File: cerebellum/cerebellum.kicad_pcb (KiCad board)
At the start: 2 copper layers, 0 parts

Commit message: [Complete cerebellum schematic
* add gd32f405vghx to library

Signed-off-by: Homalozoa X <nx.tardis@gmail.com>
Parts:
- added C1: 20pF, 10%, 10V, Capacitor_SMD:C_0402_1005Metric, B.Cu at (138.7, 115.8)
- added C10: 100nF, 10%, 10V, Capacitor_SMD:C_0402_1005Metric, B.Cu at (136.1, 106.1)
- added C11: 10uF, 10%, 10V, Capacitor_SMD:C_0402_1005Metric, B.Cu at (137.5, 122.5)
- added C12: 100nF, 10%, 10V, Capacitor_SMD:C_0402_1005Metric, B.Cu at (138.6, 122.5)
- added C13: 4.7uF 50V, Capacitor_SMD:C_0805_2012Metric, B.Cu at (121.2, 78.4)
- added C14: 10pF, 10%, 50V, Capacitor_SMD:C_0402_1005Metric, B.Cu at (125.8, 113.3)
- added C15: 10pF, 10%, 50V, Capacitor_SMD:C_0402_1005Metric, B.Cu at (125.8, 108.2)
- added C16: 10nF, 10%, 50V, Capacitor_SMD:C_0402_1005Metric, B.Cu at (119.1, 107.8)
- added C17: 10nf 50V, Capacitor_SMD:C_0402_1005Metric, B.Cu at (124.3, 98.7)
- added C18: 470nF, 10%, 50V, Capacitor_SMD:C_0603_1608Metric, B.Cu at (123.3, 107.7)
- added C19: 100uf 50V, Capacitor_SMD:C_0805_2012Metric, B.Cu at (120.7, 100.2)
- added C2: 100nF, 10%, 10V, Capacitor_SMD:C_0402_1005Metric, B.Cu at (138.0, 113.4)
- added C20: 100nf 10V, Capacitor_SMD:C_0402_1005Metric, B.Cu at (136.1, 109.2)
- added C21: 1.5nf 50V, Capacitor_SMD:C_0402_1005Metric, B.Cu at (117.1, 96.9)
- added C22: 100pF, 10%, 10V, Capacitor_SMD:C_0402_1005Metric, B.Cu at (116.4, 111.9)
- added C23: 100pF, 10%, 10V, Capacitor_SMD:C_0402_1005Metric, B.Cu at (116.4, 109.2)
- added C24: 100nf 50V, Capacitor_SMD:C_0402_1005Metric, B.Cu at (118.1, 98.8)
- added C25: 100nF, 10%, 50V, Capacitor_SMD:C_0402_1005Metric, B.Cu at (120.2, 105.8)
- added C26: 10uF, 10%, 50V, Capacitor_SMD:C_0603_1608Metric, B.Cu at (119.8, 104.5)
- added C27: 10uF, 10%, 50V, Capacitor_SMD:C_0603_1608Metric, B.Cu at (123.3, 106.2)
- added C28: 150pf 50V, Capacitor_SMD:C_0402_1005Metric, B.Cu at (115.0, 98.9)
- added C29: 4.7uF, 10%, 10V, Capacitor_SMD:C_0402_1005Metric, B.Cu at (177.8, 102.8)
- added C3: 20pF, 10%, 10V, Capacitor_SMD:C_0402_1005Metric, B.Cu at (138.8, 120.9)
- added C30: 100nF, 10%, 10V, Capacitor_SMD:C_0402_1005Metric, B.Cu at (176.7, 102.8)
- added C31: 4.7uF, 10%, 10V, Capacitor_SMD:C_0402_1005Metric, B.Cu at (120.6, 119.5)
- added C32: 100nF, 10%, 10V, Capacitor_SMD:C_0402_1005Metric, B.Cu at (120.6, 118.2)
- added C4: 100nF, 10%, 10V, Capacitor_SMD:C_0402_1005Metric, B.Cu at (136.0, 112.3)
- added C5: 100nF, 10%, 10V, Capacitor_SMD:C_0402_1005Metric, B.Cu at (136.0, 111.3)
- added C6: 4.7uF, 10%, 10V, Capacitor_SMD:C_0402_1005Metric, B.Cu at (136.0, 110.3)
- added C7: 1uF, 10%, 10V, Capacitor_SMD:C_0402_1005Metric, B.Cu at (136.1, 107.2)
- added C8: 100nF, 10%, 10V, Capacitor_SMD:C_0402_1005Metric, B.Cu at (136.1, 108.2)
- added C9: 10uF, 10%, 10V, Capacitor_SMD:C_0402_1005Metric, B.Cu at (136.1, 105.1)
- added D1: 30V, Diode_SMD:D_SMA, B.Cu at (121.3, 81.2)
- added D2: B340, Diode_SMD:D_SMC, B.Cu at (129.3, 96.7)
- added D3: 12V, Diode_SMD:D_SOD-323, B.Cu at (114.9, 112.5)
- added D4: 12V, Diode_SMD:D_SOD-323, B.Cu at (114.9, 108.5)
- added J1: PWR_OUT, Rolling_Custom:XT30PW(2+2), F.Cu at (119.3, 85.9)
- added J2: PWR_IN, Rolling_Custom:XT30PW(2+2), F.Cu at (134.0, 85.9)
- added J3: Conn_01x04, Connector_PinHeader_1.27mm:PinHeader_1x04_P1.27mm_Vertical, F.Cu at (157.2, 76.0)
- added J4: gh1.25, 3p, Connector_JST:JST_GH_SM03B-GHS-TB_1x03-1MP_P1.25mm_Horizontal, F.Cu at (148.5, 77.6)
- added L1: 20R, Resistor_SMD:R_0402_1005Metric, B.Cu at (137.0, 124.0)
- added L2: 15uh, Inductor_SMD:L_0603_1608Metric, B.Cu at (124.1, 100.0)
- added Q1: AP2300, Package_TO_SOT_SMD:SOT-23, B.Cu at (172.8, 104.7)
- added R1: 10k, 5%, Resistor_SMD:R_0402_1005Metric, B.Cu at (136.0, 113.4)
- added R10: 10k, Resistor_SMD:R_0402_1005Metric, B.Cu at (175.5, 103.9)
- added R11: 549R, Resistor_SMD:R_0201_0603Metric, B.Cu at (116.0, 98.7)
- added R12: 33R/1%, Resistor_SMD:R_0805_2012Metric, B.Cu at (172.9, 93.3)
- added R13: 33R/1%, Resistor_SMD:R_0805_2012Metric, B.Cu at (177.3, 89.4)
- added R14: 33R/1%, Resistor_SMD:R_0805_2012Metric, B.Cu at (177.4, 97.2)
- added R15: 33R/1%, Resistor_SMD:R_0805_2012Metric, B.Cu at (181.8, 93.3)
- added R2: 10k, 5%, Resistor_SMD:R_0402_1005Metric, B.Cu at (133.2, 113.5)
- added R3: 0, Resistor_SMD:R_0402_1005Metric, B.Cu at (139.6, 122.5)
- added R4: 33k, Resistor_SMD:R_0402_1005Metric, B.Cu at (117.4, 106.8)
- added R5: 3k, Resistor_SMD:R_0402_1005Metric, B.Cu at (120.1, 106.8)
- added R6: 10k, Resistor_SMD:R_0402_1005Metric, B.Cu at (118.1, 96.9)
- added R7: 5.9k, Resistor_SMD:R_0402_1005Metric, B.Cu at (116.0, 96.9)
- added R9: 100R, Resistor_SMD:R_0402_1005Metric, B.Cu at (173.0, 102.3)
- added U1: GD32F405VGHx, Package_BGA:UFBGA-100_7x7mm_Layout12x12_P0.5mm, B.Cu at (132.4, 118.6)
- added U2: TPS5430DDAR, Rolling_Custom:TPS5430DDAR, B.Cu at (121.5, 93.7)
- added U3: BMI088, Rolling_Custom:PQFN50P450X300X100-16N, B.Cu at (177.4, 93.3)
- added U4: TCAN4550RGYRQ1, Rolling_Custom:VQFN20, B.Cu at (120.7, 110.7)
- added U5: ICP-20100, Rolling_Custom:PQFN50P200X200X85-10N, B.Cu at (120.3, 121.5)
- added Y1: 8M, Oscillator:Oscillator_SMD_EuroQuartz_XO32-4Pin_3.2x2.5mm, B.Cu at (138.7, 118.3)
- added Y2: 40M, Oscillator:Oscillator_SMD_EuroQuartz_XO32-4Pin_3.2x2.5mm, B.Cu at (125.8, 110.7)
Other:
- board outline added: 91.5 x 52 mm

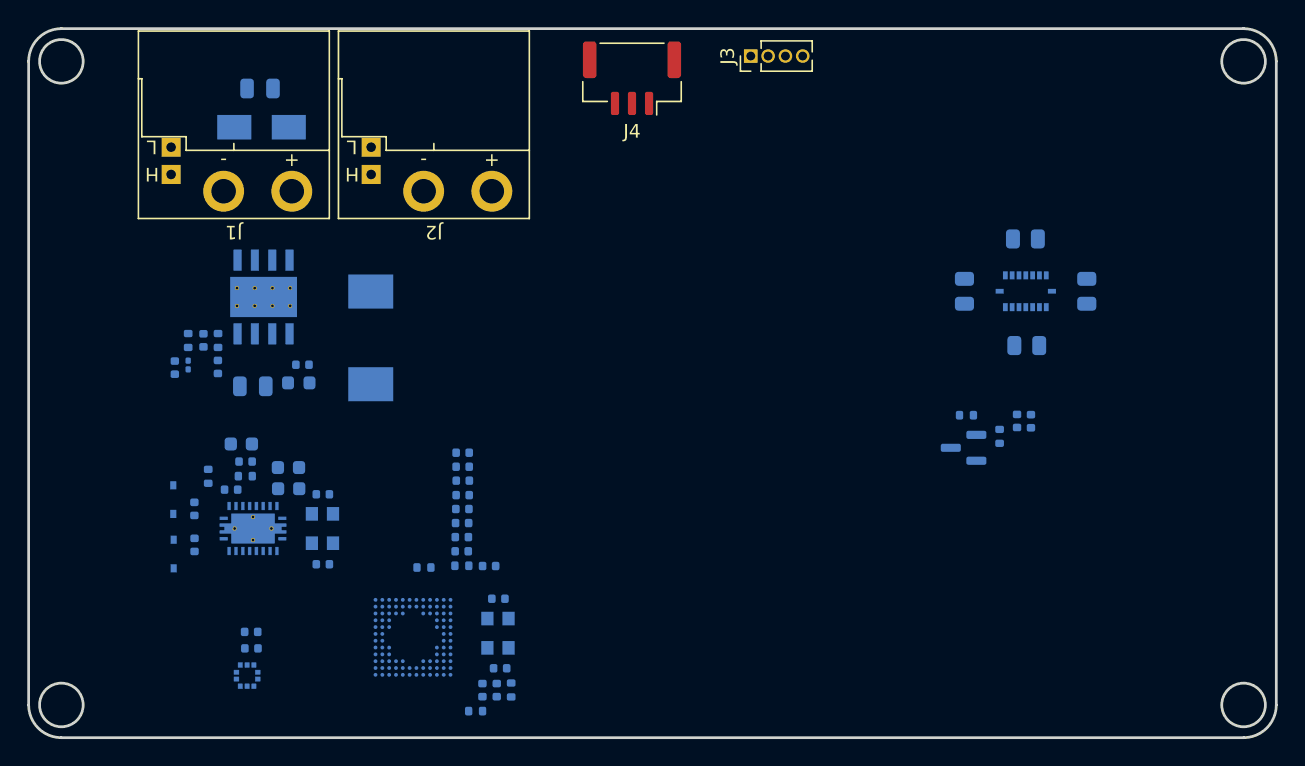
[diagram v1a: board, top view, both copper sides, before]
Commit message: [New] Add cm4 to cerebellum
Signed-off-by: Homalozoa X <nx.tardis@gmail.com>
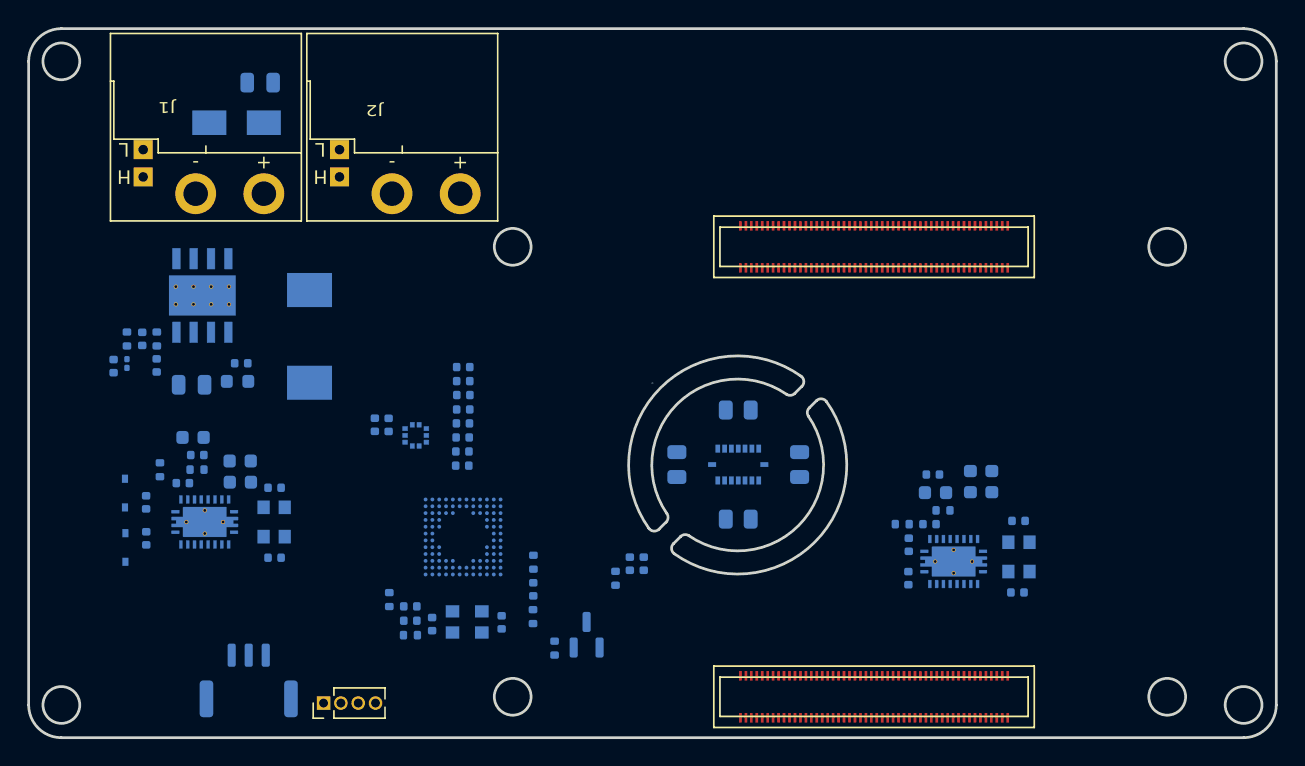
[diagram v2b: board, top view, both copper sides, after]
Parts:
- added C33: 10pF, 10%, 50V, Capacitor_SMD:C_0402_1005Metric, B.Cu at (176.8, 115.3)
- added C34: 10pF, 10%, 50V, Capacitor_SMD:C_0402_1005Metric, B.Cu at (176.8, 110.1)
- added C35: 10nF, 10%, 50V, Capacitor_SMD:C_0402_1005Metric, B.Cu at (170.3, 110.3)
- added C36: 470nF, 10%, 50V, Capacitor_SMD:C_0603_1608Metric, B.Cu at (174.9, 107.2)
- added C37: 100pF, 10%, 10V, Capacitor_SMD:C_0402_1005Metric, B.Cu at (168.8, 114.3)
- added C38: 100pF, 10%, 10V, Capacitor_SMD:C_0402_1005Metric, B.Cu at (168.8, 111.8)
- added C39: 100nF, 10%, 50V, Capacitor_SMD:C_0402_1005Metric, B.Cu at (170.6, 106.7)
- added C40: 10uF, 10%, 50V, Capacitor_SMD:C_0603_1608Metric, B.Cu at (170.8, 108.0)
- added C41: 10uF, 10%, 50V, Capacitor_SMD:C_0603_1608Metric, B.Cu at (173.3, 107.2)
- added J5: DF40C-100DS-0.4V(51), Rolling_Custom:HRS_DF40C-100DS-0.4V(51), F.Cu at (166.2, 123.0)
- added J6: DF40C-100DS-0.4V(51), Rolling_Custom:HRS_DF40C-100DS-0.4V(51), F.Cu at (166.2, 90.0)
- added R16: 3k, Resistor_SMD:R_0402_1005Metric, B.Cu at (171.3, 109.3)
- added R8: 33k, Resistor_SMD:R_0402_1005Metric, B.Cu at (168.3, 110.3)
- added U7: TCAN4550RGYRQ1, Rolling_Custom:VQFN20, B.Cu at (172.1, 113.1)
- added Y3: 40M, Oscillator:Oscillator_SMD_EuroQuartz_XO32-4Pin_3.2x2.5mm, B.Cu at (176.9, 112.7)
- J4: moved to B.Cu
- moved J3 56.9 mm to (125.9, 123.5)
- moved J4 52.4 mm to (120.4, 121.8)
- moved R9 34.7 mm to (142.8, 119.4), turned to 90 degrees
- moved Q1 30.9 mm to (145.2, 118.5), turned to 90 degrees
- moved C30 30.3 mm to (148.3, 113.2)
- moved C29 30.3 mm to (149.4, 113.2)
- moved R10 30.0 mm to (147.3, 114.3)
- moved R13 29.4 mm to (156.3, 110.0), turned to 180 degrees
- moved U3 24.6 mm to (156.3, 106.0)
- moved R12 24.6 mm to (151.8, 106.0)
- moved R15 24.6 mm to (160.8, 106.0)
- moved R14 21.7 mm to (156.3, 102.0), turned to 0 degrees
- moved U5 21.5 mm to (132.6, 103.8), turned to -90 degrees
- moved C31 19.2 mm to (130.7, 103.1), turned to -90 degrees
- moved C32 17.7 mm to (129.6, 103.0), turned to -90 degrees
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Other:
- outline, holes or cut-outs redrawn
- copper layers 2 -> 4

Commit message: [New] NC serveral pins of CM4 & Add uPD720201
Signed-off-by: Homalozoa X <nx.tardis@gmail.com>
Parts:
- moved C38 33.0 mm to (159.3, 80.2), turned to -90 degrees
- moved C33 31.3 mm to (168.5, 85.2)
- moved C35 31.3 mm to (162.0, 80.2)
- moved C36 31.3 mm to (166.6, 77.1)
- moved C39 31.3 mm to (162.3, 76.5)
- moved C40 31.3 mm to (162.5, 77.9)
- moved C41 31.3 mm to (165.0, 77.1)
- moved C34 31.3 mm to (168.6, 80.0)
- moved R16 31.3 mm to (163.0, 79.2)
- moved U7 31.3 mm to (163.8, 82.9)
- moved Y3 31.3 mm to (168.6, 82.6)
- moved C37 30.5 mm to (159.4, 85.3), turned to 90 degrees
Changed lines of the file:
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@@
   )
   (footprint "Capacitor_SMD:C_0402_1005Metric" (layer "B.Cu")
-    (at 170.3175 110.34)
+    (at 162.03 80.19)
     (descr "Capacitor SMD 0402 (1005 Metric), square (rectangular) end terminal, IPC_7351 nominal, (Body size source: IPC-SM-782 page 76, https://www.pcb-3d.com/wordpress/wp-content/uploads/ipc-sm-782a_amendment_1_and_2.pdf), generated with kicad-footprint-generator")
     (tags "capacitor")
@@
   )
   (footprint "Resistor_SMD:R_0402_1005Metric" (layer "B.Cu")
-    (at 171.3075 109.33 180)
+    (at 163.02 79.18 180)
     (descr "Resistor SMD 0402 (1005 Metric), square (rectangular) end terminal, IPC_7351 nominal, (Body size source: IPC-SM-782 page 72, https://www.pcb-3d.com/wordpress/wp-content/uploads/ipc-sm-782a_amendment_1_and_2.pdf), generated with kicad-footprint-generator")
     (tags "resistor")
@@
   )
   (footprint "Oscillator:Oscillator_SMD_EuroQuartz_XO32-4Pin_3.2x2.5mm" (layer "B.Cu")
-    (at 176.8775 112.74)
+    (at 168.59 82.59)
     (descr "Miniature Crystal Clock Oscillator EuroQuartz XO32 series, http://cdn-reichelt.de/documents/datenblatt/B400/XO32.pdf, 3.2x2.5mm^2 package")
     (tags "SMD SMT crystal oscillator")
@@
   )
   (footprint "Rolling_Custom:VQFN20" (layer "B.Cu")
-    (at 172.09 113.08 90)
+    (at 163.8025 82.93 90)
     (property "MANUFACTURER" "Texas Instruments")
     (property "MAXIMUM_PACKAGE_HEIGHT" "1 mm")
@@
       (effects (font (size 1 1) (thickness 0.15)) (justify mirror))
     )
-    (fp_text user "${REFERENCE}" (at 0 0) (layer "B.SilkS")
+    (fp_text user "${REFERENCE}" (at 0.0075 -0.06) (layer "B.SilkS")
       (effects (font (size 0.8 0.26) (thickness 0.04)) (justify mirror))
     )
@@
   )
   (footprint "Capacitor_SMD:C_0402_1005Metric" (layer "B.Cu")
-    (at 176.8475 110.1)
+    (at 168.56 79.95)
     (descr "Capacitor SMD 0402 (1005 Metric), square (rectangular) end terminal, IPC_7351 nominal, (Body size source: IPC-SM-782 page 76, https://www.pcb-3d.com/wordpress/wp-content/uploads/ipc-sm-782a_amendment_1_and_2.pdf), generated with kicad-footprint-generator")
     (tags "capacitor")
@@
   )
   (footprint "Capacitor_SMD:C_0603_1608Metric" (layer "B.Cu")
-    (at 174.8875 107.22 90)
+    (at 166.6 77.07 90)
     (descr "Capacitor SMD 0603 (1608 Metric), square (rectangular) end terminal, IPC_7351 nominal, (Body size source: IPC-SM-782 page 76, https://www.pcb-3d.com/wordpress/wp-content/uploads/ipc-sm-782a_amendment_1_and_2.pdf), generated with kicad-footprint-generator")
     (tags "capacitor")
@@
   )
   (footprint "Capacitor_SMD:C_0402_1005Metric" (layer "B.Cu")
-    (at 176.7675 115.35 180)
+    (at 168.48 85.2 180)
     (descr "Capacitor SMD 0402 (1005 Metric), square (rectangular) end terminal, IPC_7351 nominal, (Body size source: IPC-SM-782 page 76, https://www.pcb-3d.com/wordpress/wp-content/uploads/ipc-sm-782a_amendment_1_and_2.pdf), generated with kicad-footprint-generator")
     (tags "capacitor")
@@
   )
   (footprint "Capacitor_SMD:C_0402_1005Metric" (layer "B.Cu")
-    (at 170.5675 106.7 180)
+    (at 162.28 76.55 180)
     (descr "Capacitor SMD 0402 (1005 Metric), square (rectangular) end terminal, IPC_7351 nominal, (Body size source: IPC-SM-782 page 76, https://www.pcb-3d.com/wordpress/wp-content/uploads/ipc-sm-782a_amendment_1_and_2.pdf), generated with kicad-footprint-generator")
     (tags "capacitor")
@@
   )
   (footprint "Capacitor_SMD:C_0402_1005Metric" (layer "B.Cu")
-    (at 168.7675 114.3 -90)
+    (at 159.36 85.33 90)
     (descr "Capacitor SMD 0402 (1005 Metric), square (rectangular) end terminal, IPC_7351 nominal, (Body size source: IPC-SM-782 page 76, https://www.pcb-3d.com/wordpress/wp-content/uploads/ipc-sm-782a_amendment_1_and_2.pdf), generated with kicad-footprint-generator")
     (tags "capacitor")
@@
     (property "Sheetname" "")
     (attr smd)
-    (fp_text reference "C37" (at 2.35 0.09 90) (layer "B.SilkS")
+    (fp_text reference "C37" (at 0.84 1.1 90) (layer "B.SilkS")
       (effects (font (size 0.8 1) (thickness 0.15)) (justify mirror))
     )
@@
     (fp_line (start -0.5 0.25) (end 0.5 0.25) (layer "B.Fab") (width 0.1))
     (fp_line (start 0.5 0.25) (end 0.5 -0.25) (layer "B.Fab") (width 0.1))
-    (pad "1" smd roundrect (at -0.48 0 270) (size 0.56 0.62) (layers "B.Cu" "B.Paste" "B.Mask") (roundrect_rratio 0.25)
+    (pad "1" smd roundrect (at -0.48 0 90) (size 0.56 0.62) (layers "B.Cu" "B.Paste" "B.Mask") (roundrect_rratio 0.25)
       (net 1 "GND") (pintype "passive"))
-    (pad "2" smd roundrect (at 0.48 0 270) (size 0.56 0.62) (layers "B.Cu" "B.Paste" "B.Mask") (roundrect_rratio 0.25)
+    (pad "2" smd roundrect (at 0.48 0 90) (size 0.56 0.62) (layers "B.Cu" "B.Paste" "B.Mask") (roundrect_rratio 0.25)
       (net 16 "CAN_L") (pintype "passive"))
     (model "${KICAD6_3DMODEL_DIR}/Capacitor_SMD.3dshapes/C_0402_1005Metric.wrl"
@@
   )
   (footprint "Capacitor_SMD:C_0402_1005Metric" (layer "B.Cu")
-    (at 168.7975 111.85 90)
+    (at 159.34 80.21 -90)
     (descr "Capacitor SMD 0402 (1005 Metric), square (rectangular) end terminal, IPC_7351 nominal, (Body size source: IPC-SM-782 page 76, https://www.pcb-3d.com/wordpress/wp-content/uploads/ipc-sm-782a_amendment_1_and_2.pdf), generated with kicad-footprint-generator")
     (tags "capacitor")
@@
     (fp_line (start 0.5 -0.25) (end -0.5 -0.25) (layer "B.Fab") (width 0.1))
     (fp_line (start 0.5 0.25) (end 0.5 -0.25) (layer "B.Fab") (width 0.1))
-    (pad "1" smd roundrect (at -0.48 0 90) (size 0.56 0.62) (layers "B.Cu" "B.Paste" "B.Mask") (roundrect_rratio 0.25)
+    (pad "1" smd roundrect (at -0.48 0 270) (size 0.56 0.62) (layers "B.Cu" "B.Paste" "B.Mask") (roundrect_rratio 0.25)
       (net 1 "GND") (pintype "passive"))
-    (pad "2" smd roundrect (at 0.48 0 90) (size 0.56 0.62) (layers "B.Cu" "B.Paste" "B.Mask") (roundrect_rratio 0.25)
+    (pad "2" smd roundrect (at 0.48 0 270) (size 0.56 0.62) (layers "B.Cu" "B.Paste" "B.Mask") (roundrect_rratio 0.25)
       (net 17 "CAN_H") (pintype "passive"))
     (model "${KICAD6_3DMODEL_DIR}/Capacitor_SMD.3dshapes/C_0402_1005Metric.wrl"
@@
   )
   (footprint "Capacitor_SMD:C_0603_1608Metric" (layer "B.Cu")
-    (at 173.3175 107.22 90)
+    (at 165.03 77.07 90)
     (descr "Capacitor SMD 0603 (1608 Metric), square (rectangular) end terminal, IPC_7351 nominal, (Body size source: IPC-SM-782 page 76, https://www.pcb-3d.com/wordpress/wp-content/uploads/ipc-sm-782a_amendment_1_and_2.pdf), generated with kicad-footprint-generator")
     (tags "capacitor")
@@
   )
   (footprint "Capacitor_SMD:C_0603_1608Metric" (layer "B.Cu")
-    (at 170.7575 108.03 180)
+    (at 162.47 77.88 180)
     (descr "Capacitor SMD 0603 (1608 Metric), square (rectangular) end terminal, IPC_7351 nominal, (Body size source: IPC-SM-782 page 76, https://www.pcb-3d.com/wordpress/wp-content/uploads/ipc-sm-782a_amendment_1_and_2.pdf), generated with kicad-footprint-generator")
     (tags "capacitor")
